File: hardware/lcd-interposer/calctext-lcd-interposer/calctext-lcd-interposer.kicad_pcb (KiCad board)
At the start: 2 copper layers, 17.5 x 16 mm, 10 parts, among them J1 HICENDA_FPC, J2 MAINBOARD_FFC

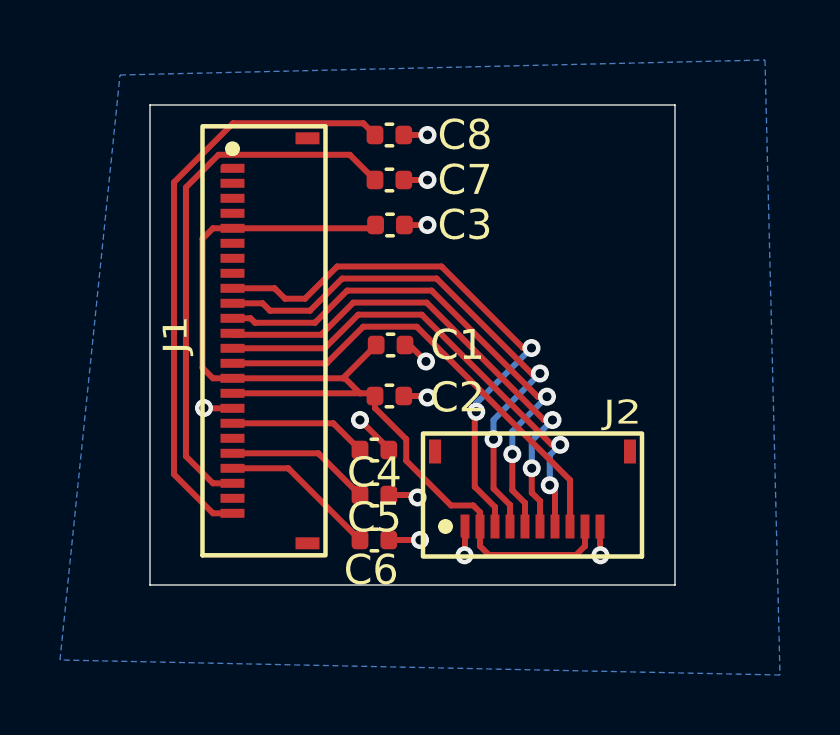
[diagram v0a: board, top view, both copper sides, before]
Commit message: Refine LCD interposer power routing
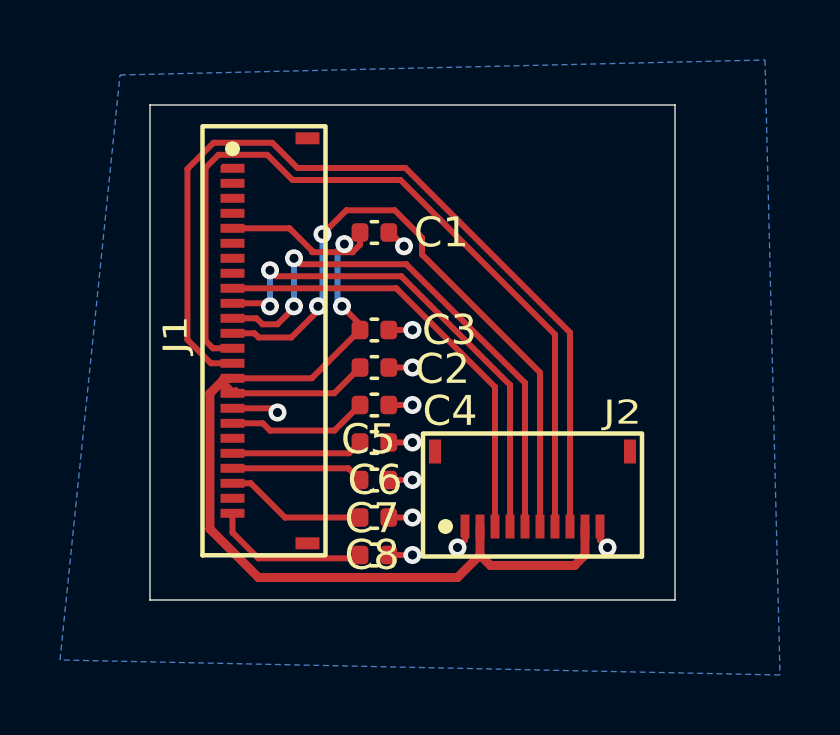
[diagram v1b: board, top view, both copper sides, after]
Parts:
- moved C8 14.0 mm to (131.0, 109.0)
- moved C7 11.3 mm to (131.0, 107.8)
- moved C1 3.79 mm to (131.0, 98.2)
- moved C3 3.54 mm to (131.0, 101.5)
- moved C6 2.00 mm to (131.0, 106.5)
- moved C5 1.75 mm to (131.0, 105.2)
- moved C4 1.50 mm to (131.0, 104.0)
- moved C2 1.07 mm to (131.0, 102.8)
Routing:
- net VGL: track 19.9 -> 5.29 mm
- net LCD_SDI: track 15.4 -> 29.7 mm
- net VNV: track 18.0 -> 4.72 mm
- net LCD_SCLK: track 16.1 -> 27.5 mm, vias 2 -> 0
- net IOVCC: track 33.5 -> 40.4 mm, vias 0 -> 2
- net LCD_CS: track 16.7 -> 21.2 mm
- net LCD_TE: track 18.7 -> 14.8 mm, vias 2 -> 0
- net LCD_RST: track 18.1 -> 16.8 mm
- net GND: track 10.4 -> 9.39 mm
- net AVDD: track 5.24 -> 4.41 mm
- net LCD_DC: track 17.4 -> 18.2 mm
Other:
- board size 17.5 x 16 mm -> 17.5 x 16.5 mm
